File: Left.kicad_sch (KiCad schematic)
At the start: 127 parts, among them J2 Conn_01x08, J4 DEBUG, J5 OLED, J6 EPAPER RIBBON, M1 M.2_Key_E, U1 XC6206P332MR

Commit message: start working on adding the db
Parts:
- added J?: Conn_01x08, Connector-pat-various:100519220810EHLF, symbol Connector_Generic:Conn_01x08
- added J?: USB_C_Receptacle_USB2.0, symbol Connector:USB_C_Receptacle_USB2.0
- added MO? (x3): MOUNTING, MountingHole:MountingHole_2.2mm_M2_Pad, symbol Mechanical:MountingHole
- added U?: SRV05-4, marbastlib-various:SOT-23-6-routable, symbol marbastlib-various:SRV05-4
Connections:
- net DI+: now also J?.1 (Pin_1)
- net DI-: now also J?.2 (Pin_2)
- net GND: now also J?.8 (Pin_8)
- net I2C1_SCL: now also J?.5 (Pin_5)
- net I2C1_SDA: now also J?.4 (Pin_4)
- net vbat: now also J?.7 (Pin_7)
- net vbus: now also J?.6 (Pin_6)
- new net: J?.A1 (GND), J?.A12 (GND), J?.B1 (GND), J?.B12 (GND)
- new net: J?.A4 (VBUS), J?.A9 (VBUS), J?.B4 (VBUS), J?.B9 (VBUS)
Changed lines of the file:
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@@
     (effects (font (size 1.27 1.27)) (justify right bottom))
+  )
+  (label "DI+" (at 361.95 54.61 0)
+    (effects (font (size 1.27 1.27)) (justify left bottom))
   )
   (label "vout" (at 86.995 57.15 180)
@@
     (effects (font (size 1.27 1.27)) (justify right bottom))
   )
+  (label "vbat" (at 361.95 69.85 0)
+    (effects (font (size 1.27 1.27)) (justify left bottom))
+  )
   (label "col2" (at 48.26 113.03 90)
     (effects (font (size 1.27 1.27)) (justify left bottom))
@@
     (effects (font (size 1.27 1.27)) (justify left bottom))
   )
+  (label "vbus" (at 361.95 67.31 0)
+    (effects (font (size 1.27 1.27)) (justify left bottom))
+  )
   (label "CS" (at 222.25 132.715 180)
     (effects (font (size 1.27 1.27)) (justify right bottom))
@@
     (effects (font (size 1.27 1.27)) (justify right bottom))
   )
+  (label "I2C1_SCL" (at 361.95 64.77 0)
+    (effects (font (size 1.27 1.27)) (justify left bottom))
+  )
   (label "DI+" (at 164.465 48.895 0)
     (effects (font (size 1.27 1.27)) (justify left bottom))
@@
     (effects (font (size 1.27 1.27)) (justify left bottom))
   )
+  (label "I2C1_SDA" (at 361.95 62.23 0)
+    (effects (font (size 1.27 1.27)) (justify left bottom))
+  )
   (label "vout" (at 136.525 43.815 180)
     (effects (font (size 1.27 1.27)) (justify right bottom))
@@
   (label "P2" (at 188.595 38.735 180)
     (effects (font (size 1.27 1.27)) (justify right bottom))
+  )
+  (label "DI-" (at 361.95 57.15 0)
+    (effects (font (size 1.27 1.27)) (justify left bottom))
   )
   (label "P5" (at 188.595 46.355 180)
@@
     (pin "2")
   )
+  (symbol (lib_id "marbastlib-various:SRV05-4") (at 320.675 61.595 0) (unit 1)
+    (in_bom yes) (on_board yes) (fields_autoplaced)
+    (property "Reference" "U?" (id 0) (at 323.4437 45.72 0)
+      (effects (font (size 1.27 1.27)) (justify left))
+    )
+    (property "Value" "SRV05-4" (id 1) (at 323.4437 48.26 0)
+      (effects (font (size 1.27 1.27)) (justify left))
+    )
+    (property "Footprint" "marbastlib-various:SOT-23-6-routable" (id 2) (at 338.455 73.025 0)
+      (effects (font (size 1.27 1.27)) hide)
+    )
+    (property "Datasheet" "http://www.onsemi.com/pub/Collateral/SRV05-4-D.PDF" (id 3) (at 320.675 61.595 0)
+      (effects (font (size 1.27 1.27)) hide)
+    )
+    (pin "1")
+    (pin "2")
+    (pin "3")
+    (pin "4")
+    (pin "5")
+    (pin "6")
+  )
   (symbol (lib_id "MX_Alps_Hybrid:MX-NoLED") (at 77.47 143.51 0) (mirror y) (unit 1)
     (in_bom yes) (on_board yes) (fields_autoplaced)
@@
     )
   )
+  (symbol (lib_id "Mechanical:MountingHole") (at 315.595 93.345 0) (unit 1)
+    (in_bom yes) (on_board yes)
+    (property "Reference" "MO?" (id 0) (at 313.69 90.17 0)
+      (effects (font (size 1.27 1.27)) (justify left))
+    )
+    (property "Value" "MOUNTING" (id 1) (at 313.69 96.52 0)
+      (effects (font (size 1.27 1.27)) (justify left))
+    )
+    (property "Footprint" "MountingHole:MountingHole_2.2mm_M2_Pad" (id 2) (at 315.595 93.345 0)
+      (effects (font (size 1.27 1.27)) hide)
+    )
+    (property "Datasheet" "~" (id 3) (at 315.595 93.345 0)
+      (effects (font (size 1.27 1.27)) hide)
+    )
+  )
   (symbol (lib_id "MX_Alps_Hybrid:MX-NoLED") (at 90.17 124.46 90) (mirror x) (unit 1)
     (in_bom yes) (on_board yes)
@@
     (pin "2")
   )
+  (symbol (lib_id "Mechanical:MountingHole") (at 304.8 93.345 0) (unit 1)
+    (in_bom yes) (on_board yes)
+    (property "Reference" "MO?" (id 0) (at 302.895 90.17 0)
+      (effects (font (size 1.27 1.27)) (justify left))
+    )
+    (property "Value" "MOUNTING" (id 1) (at 302.895 96.52 0)
+      (effects (font (size 1.27 1.27)) (justify left))
+    )
+    (property "Footprint" "MountingHole:MountingHole_2.2mm_M2_Pad" (id 2) (at 304.8 93.345 0)
+      (effects (font (size 1.27 1.27)) hide)
+    )
+    (property "Datasheet" "~" (id 3) (at 304.8 93.345 0)
+      (effects (font (size 1.27 1.27)) hide)
+    )
+  )
   (symbol (lib_id "Power:GND") (at 126.365 41.275 0) (mirror y) (unit 1)
     (in_bom yes) (on_board yes)
@@
       (effects (font (size 1.27 1.27)) hide)
     )
+  )
+  (symbol (lib_id "Connector_Generic:Conn_01x08") (at 356.87 62.23 0) (mirror y) (unit 1)
+    (in_bom yes) (on_board yes) (fields_autoplaced)
+    (property "Reference" "J?" (id 0) (at 356.87 48.26 0))
+    (property "Value" "Conn_01x08" (id 1) (at 356.87 50.8 0))
+    (property "Footprint" "Connector-pat-various:100519220810EHLF" (id 2) (at 356.87 62.23 0)
+      (effects (font (size 1.27 1.27)) hide)
+    )
+    (property "Datasheet" "~" (id 3) (at 356.87 62.23 0)
+      (effects (font (size 1.27 1.27)) hide)
+    )
+    (pin "1")
+    (pin "2")
+    (pin "3")
+    (pin "4")
+    (pin "5")
+    (pin "6")
+    (pin "7")
+    (pin "8")
   )
   (symbol (lib_id "Device:C_Small") (at 207.01 158.75 90) (unit 1)
@@
     (pin "3")
   )
+  (symbol (lib_id "Mechanical:MountingHole") (at 294.64 93.345 0) (unit 1)
+    (in_bom yes) (on_board yes)
+    (property "Reference" "MO?" (id 0) (at 292.735 90.17 0)
+      (effects (font (size 1.27 1.27)) (justify left))
+    )
+    (property "Value" "MOUNTING" (id 1) (at 292.735 96.52 0)
+      (effects (font (size 1.27 1.27)) (justify left))
+    )
+    (property "Footprint" "MountingHole:MountingHole_2.2mm_M2_Pad" (id 2) (at 294.64 93.345 0)
+      (effects (font (size 1.27 1.27)) hide)
+    )
+    (property "Datasheet" "~" (id 3) (at 294.64 93.345 0)
+      (effects (font (size 1.27 1.27)) hide)
+    )
+  )
   (symbol (lib_id "Device:C_Small") (at 86.995 60.96 0) (unit 1)
     (in_bom yes) (on_board yes)
@@
     (pin "1")
     (pin "2")
+  )
+  (symbol (lib_id "power:GND") (at 361.95 72.39 0) (unit 1)
+    (in_bom yes) (on_board yes)
+    (property "Reference" "#PWR?" (id 0) (at 361.95 78.74 0)
+      (effects (font (size 1.27 1.27)) hide)
+    )
+    (property "Value" "GND" (id 1) (at 366.395 74.295 0))
+    (property "Footprint" "" (id 2) (at 361.95 72.39 0)
+      (effects (font (size 1.27 1.27)) hide)
+    )
+    (property "Datasheet" "" (id 3) (at 361.95 72.39 0)
+      (effects (font (size 1.27 1.27)) hide)
+    )
+    (pin "1")
   )
   (symbol (lib_id "MX_Alps_Hybrid:MX-NoLED") (at 64.77 162.56 90) (mirror x) (unit 1)
@@
     (pin "4")
   )
+  (symbol (lib_id "Connector:USB_C_Receptacle_USB2.0") (at 267.335 60.325 0) (unit 1)
+    (in_bom yes) (on_board yes) (fields_autoplaced)
+    (property "Reference" "J?" (id 0) (at 267.335 36.83 0))
+    (property "Value" "USB_C_Receptacle_USB2.0" (id 1) (at 267.335 39.37 0))
+    (property "Footprint" "" (id 2) (at 271.145 60.325 0)
+      (effects (font (size 1.27 1.27)) hide)
+    )
+    (property "Datasheet" "https://www.usb.org/sites/default/files/documents/usb_type-c.zip" (id 3) (at 271.145 60.325 0)
+      (effects (font (size 1.27 1.27)) hide)
+    )
+    (pin "A1")
+    (pin "A12")
+    (pin "A4")
+    (pin "A5")
+    (pin "A6")
+    (pin "A7")
+    (pin "A8")
+    (pin "A9")
+    (pin "B1")
+    (pin "B12")
+    (pin "B4")
+    (pin "B5")
+    (pin "B6")
+    (pin "B7")
+    (pin "B8")
+    (pin "B9")
+    (pin "S1")
+  )
   (symbol (lib_id "Device:D_Schottky_Small") (at 207.01 155.575 0) (unit 1)

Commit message: db stuff and spi pin deciding spreadsheet
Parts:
- removed J?: USB_C_Receptacle_USB2.0, symbol Connector:USB_C_Receptacle_USB2.0
- removed U?: SRV05-4, marbastlib-various:SOT-23-6-routable, symbol marbastlib-various:SRV05-4
- added F1: Polyfuse, Resistor_SMD:R_0805_2012Metric, symbol Device:Polyfuse
- added J1: HRO-TYPEC-M12, Connector_USB:USB_C_Receptacle_HRO_TYPE-C-31-M-12, symbol Connector:USB_C_Receptacle_USB2.0
- added J3: BATTERY, Connector_JST:JST_PH_S2B-PH-SM4-TB_1x02-1MP_P2.00mm_Horizontal, symbol Connector_Generic:Conn_01x02
- added J8: SPLIT, Connector-pat-various:Magnetic Pogo 4 pin, symbol Connector_Generic:Conn_01x04
- added R1, R2: 5.1k, Resistor_SMD:R_0402_1005Metric, symbol Device:R
- added U2: SRV05-4, Package_TO_SOT_SMD:SOT-23-6, symbol Power_Protection:SRV05-4
- J2: value Conn_01x08 -> DB FFC
- J7: renamed from J?; value Conn_01x08 -> DB FFC
- gave numbers to parts that had none: 3
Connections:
- net DI+: no longer J7.1 (Pin_1)
- net DI-: no longer J7.2 (Pin_2)
- net GND: now also J2.3 (Pin_3), J7.3 (Pin_3), J1.A1 (GND), J1.A12 (GND), J1.B1 (GND), J1.B12 (GND), J1.S1 (SHIELD), J3.2 (Pin_2), J8.4 (Pin_4), R1.1, R2.2, U2.2 (VN)
- net I2C1_SCL: no longer J7.5 (Pin_5)
- net I2C1_SDA: no longer J7.4 (Pin_4)
- net rgbin: now also UG3.3 (DIN); no longer UG9.3 (DIN)
- net vbat: no longer J7.7 (Pin_7)
- net vbus: no longer J7.6 (Pin_6)
- net at UG2.1 (DOUT): now also UG1.3 (DIN); no longer UG3.3 (DIN)
- net at UG2.3 (DIN): now also UG3.1 (DOUT); no longer UG1.1 (DOUT)
- net at R5.1, UG1.4 (VDD), UG2.4 (VDD)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: now also UG9.4 (VDD)
- net at UG7.1 (DOUT): now also UG9.3 (DIN); no longer UG6.3 (DIN)
- net at UG7.3 (DIN): now also UG6.1 (DOUT); no longer UG9.1 (DOUT)
- net at UG4.1 (DOUT): now also UG5.3 (DIN); no longer UG1.3 (DIN)
- net at UG4.3 (DIN): now also UG1.1 (DOUT); no longer UG5.1 (DOUT)
- new net: F1.2, J1.A4 (VBUS), J1.A9 (VBUS), J1.B4 (VBUS), J1.B9 (VBUS)
- new net: J1.A5 (CC1), R1.2
- new net: J1.B5 (CC2), R2.1
- new net: UG5.1 (DOUT), UG6.3 (DIN)
- new net BATT+: J3.1 (Pin_1), J7.7 (Pin_7)
- new net D+: J1.A6 (D+), J1.B6 (D+), J7.1 (Pin_1), U2.1 (IO1)
- new net D-: J1.A7 (D-), J1.B7 (D-), J7.2 (Pin_2), U2.3 (IO2)
- new net DB_VCC: F1.1, J7.6 (Pin_6), J8.1 (Pin_1), U2.5 (VP)
- new net SPLIT_SCL: J7.5 (Pin_5), J8.2 (Pin_2)
- new net SPLIT_SDA: J7.4 (Pin_4), J8.3 (Pin_3)
- no-connect marks 4 -> 6
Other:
- note added: "ESD"
- note added: "Usb C"
- moved on the sheet: J7, MO10, MO11, MO9

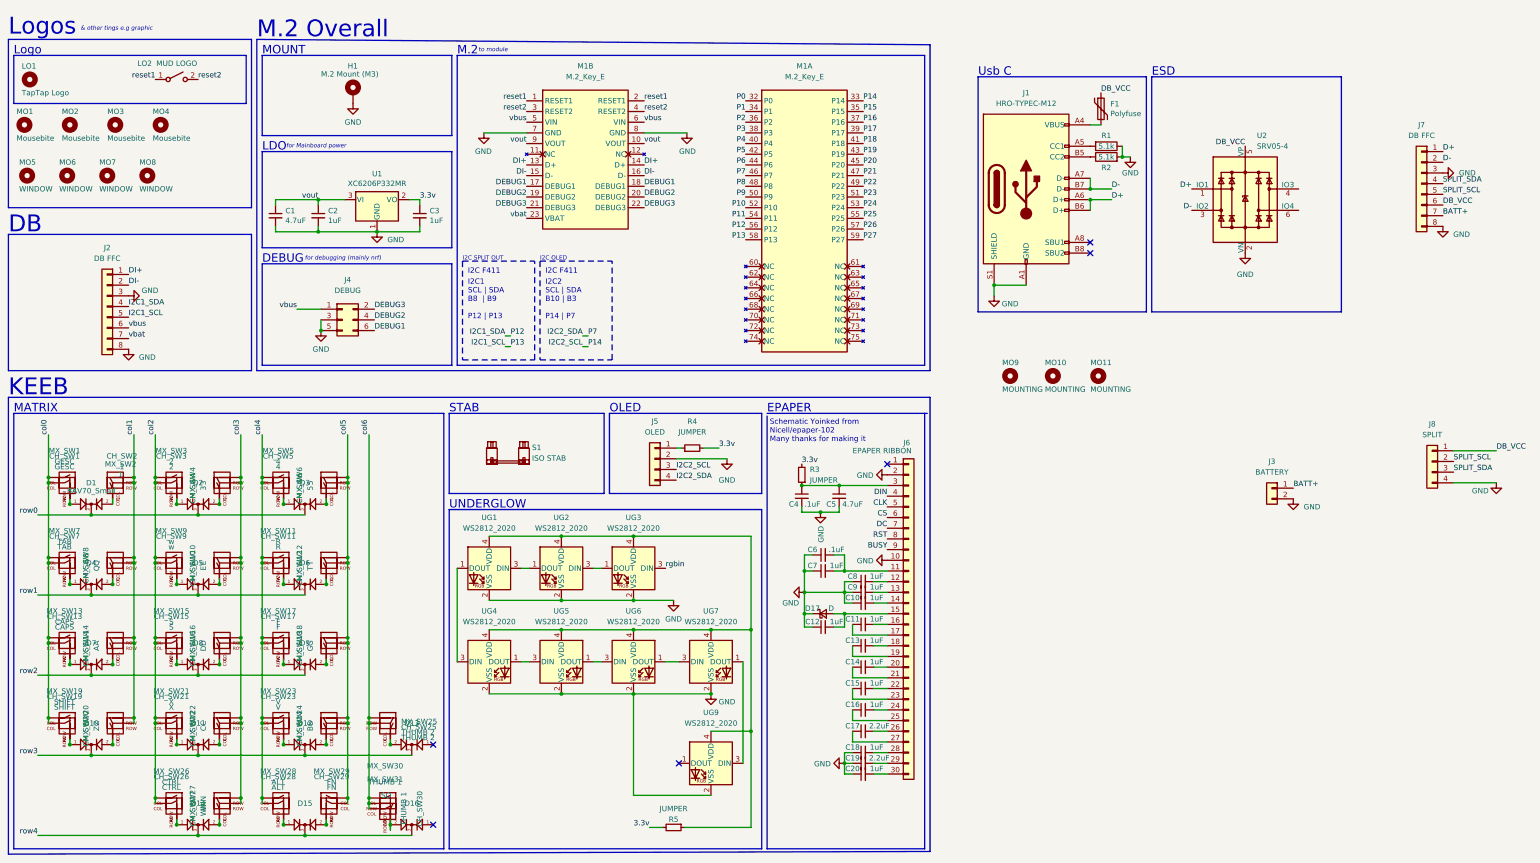
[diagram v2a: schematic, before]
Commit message: finish left side. do a bunch of right side. do right db. change db flat ribbon on both
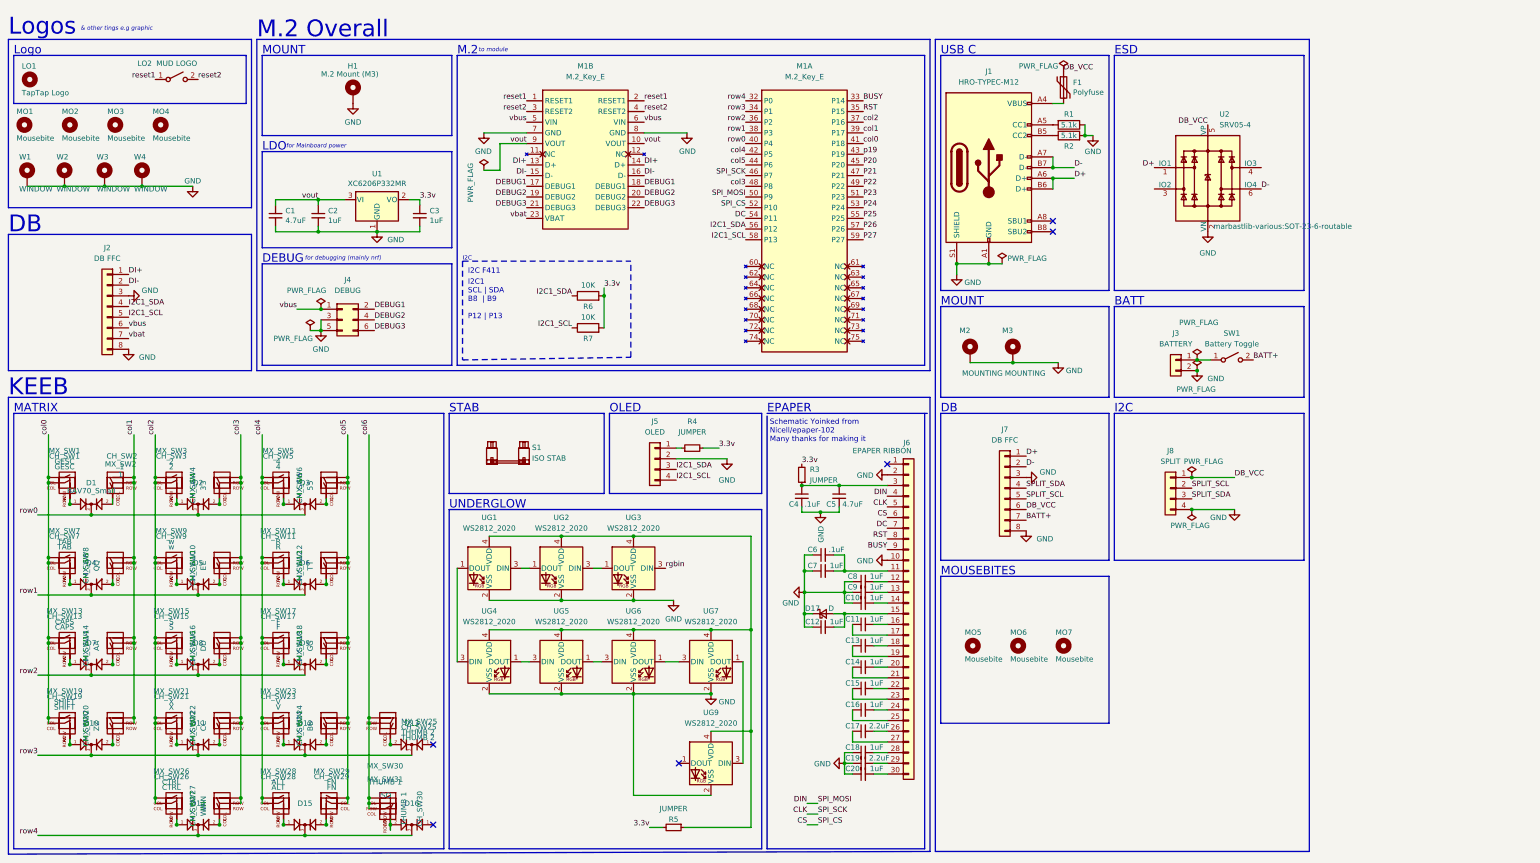
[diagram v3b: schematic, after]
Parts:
- removed MO11: MOUNTING, MountingHole:MountingHole_2.2mm_M2_Pad, symbol Mechanical:MountingHole
- removed MO8: WINDOW, MountingHole:MountingHole_2.2mm_M2_Pad, symbol Mechanical:MountingHole
- added MO5: Mousebite, marbastlib-various:mousebites_2mm, symbol Mechanical:MountingHole
- added R6, R7: 10K, Resistor_SMD:R_0402_1005Metric, symbol Device:R
- added SW1: Battery Toggle, marbastlib-various:SW_MSK12C02-HB, symbol Switch:SW_SPST
- added W2, W3, W4: WINDOW, MountingHole:MountingHole_2.2mm_M2_Pad, symbol Mechanical:MountingHole_Pad
- J1: footprint Connector_USB:USB_C_Receptacle_HRO_TYPE-C-31-M-12 -> marbastlib-various:USB_C_Receptacle_HRO_TYPE-C-31-M-14
- M2: renamed from MO9; symbol Mechanical:MountingHole -> Mechanical:MountingHole_Pad
- M3: renamed from MO10; symbol Mechanical:MountingHole -> Mechanical:MountingHole_Pad
- MO6, MO7: value WINDOW -> Mousebite; footprint MountingHole:MountingHole_2.2mm_M2_Pad -> marbastlib-various:mousebites_2mm
- U2: footprint Package_TO_SOT_SMD:SOT-23-6 -> marbastlib-various:SOT-23-6-routable
- W1: renamed from MO5; symbol Mechanical:MountingHole -> Mechanical:MountingHole_Pad
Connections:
- net P0 is gone; now on net row4: M1.32 (P0)
- net P1 is gone; now on net row3: M1.34 (P1)
- net P10 is gone; now on net CS: M1.52 (P10)
- net P11 is gone; now on net DC: M1.54 (P11)
- net P15 is gone; now on net RST: M1.35 (P15)
- net P16 is gone; now on net col2: M1.37 (P16)
- net P17 is gone; now on net col1: M1.39 (P17)
- net P18 is gone; now on net col0: M1.41 (P18)
- net P2 is gone; now on net row2: M1.36 (P2)
- net P3 is gone; now on net row1: M1.38 (P3)
- net P4 is gone; now on net row0: M1.40 (P4)
- net P5 is gone; now on net col4: M1.42 (P5)
- net P6 is gone; now on net col5: M1.44 (P6)
- net P8 is gone; now on net col3: M1.48 (P8)
- net P9 is gone; now on net DIN: M1.50 (P9)
- net 3.3v: now also R6.2, R7.2
- net BATT+: now also SW1.2 (B); no longer J3.1 (Pin_1)
- net BUSY: now also M1.33 (P14)
- net CLK: now also M1.46 (P7)
- net D-: now also U2.6 (IO4); no longer U2.3 (IO2)
- net DEBUG1: now also J4.2 (Pin_2); no longer J4.6 (Pin_6)
- net DEBUG3: now also J4.6 (Pin_6); no longer J4.2 (Pin_2)
- net GND: now also M2.1, M3.1, W1.1, W2.1, W3.1, W4.1
- net I2C1_SCL: now also J5.4 (Pin_4), R7.1
- net I2C1_SDA: now also J5.3 (Pin_3), R6.1
- removed net I2C2_SCL: J5.3 (Pin_3), M1.33 (P14)
- removed net I2C2_SDA: J5.4 (Pin_4), M1.46 (P7)
- net P19 renamed p19
- new net: J3.1 (Pin_1), SW1.1 (A)
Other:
- note added: "BATT"
- note added: "I2C"
- note added: "MOUSEBITES"
- note added: "USB C"
- note removed: "I2C OLED"
- note removed: "I2C SPLIT OUT"
- note removed: "I2C2 SCL | SDA B10 | B3 P14 | P7"
- note removed: "Usb C"
- moved on the sheet: F1, J1, J3, J7, J8, R1, R2, U2

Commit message: finish right. fix some things on left. add teardrops
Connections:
- net p19 is gone; now on net rgbin: M1.43 (P19)
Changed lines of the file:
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@@
     (effects (font (size 1.27 1.27)) (justify right bottom))
+  )
+  (label "rgbin" (at 216.535 46.355 0)
+    (effects (font (size 1.27 1.27)) (justify left bottom))
   )
   (label "col3" (at 188.595 53.975 180)
@@
     (effects (font (size 1.27 1.27)) (justify right bottom))
   )
-  (label "p19" (at 216.535 46.355 0)
-    (effects (font (size 1.27 1.27)) (justify left bottom))
-  )
   (label "col1" (at 216.535 41.275 0)

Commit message: add nicer logos and shit
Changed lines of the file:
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@@
       (effects (font (size 1.27 1.27)) (justify left))
     )
-    (property "Footprint" "marbastlib-various:SOT-23-6-routable" (id 2) (at 316.23 63.5 0))
+    (property "Footprint" "marbastlib-various:SOT-23-6-routable" (id 2) (at 316.23 63.5 0)
+      (effects (font (size 1.27 1.27)) hide)
+    )
     (property "Datasheet" "http://www.onsemi.com/pub/Collateral/SRV05-4-D.PDF" (id 3) (at 298.45 52.07 0)
       (effects (font (size 1.27 1.27)) hide)
